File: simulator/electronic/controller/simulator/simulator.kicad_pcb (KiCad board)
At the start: 2 copper layers, 86.9 x 70.1 mm, 57 parts, among them J1 Conn_01x03_Socket, J2 Conn_01x04_Socket, J3 Conn_01x03_Socket, J4 Conn_01x04_Socket, J5 Conn_01x03_Socket, J6 Conn_01x04_Socket, J7 Conn_01x03_Socket, J8 Conn_01x04_Socket, U1 ESP32 D1 Mini

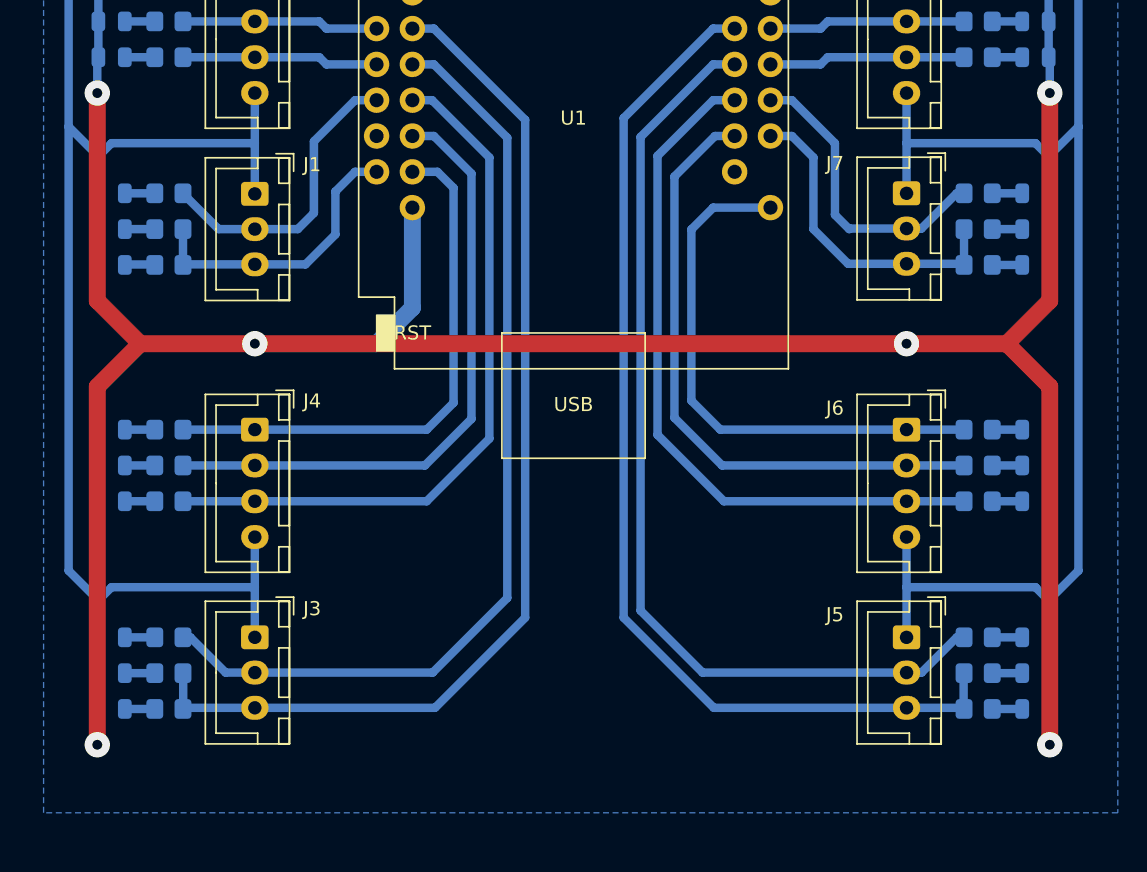
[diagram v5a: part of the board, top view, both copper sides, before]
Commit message: update Platine (Vais)
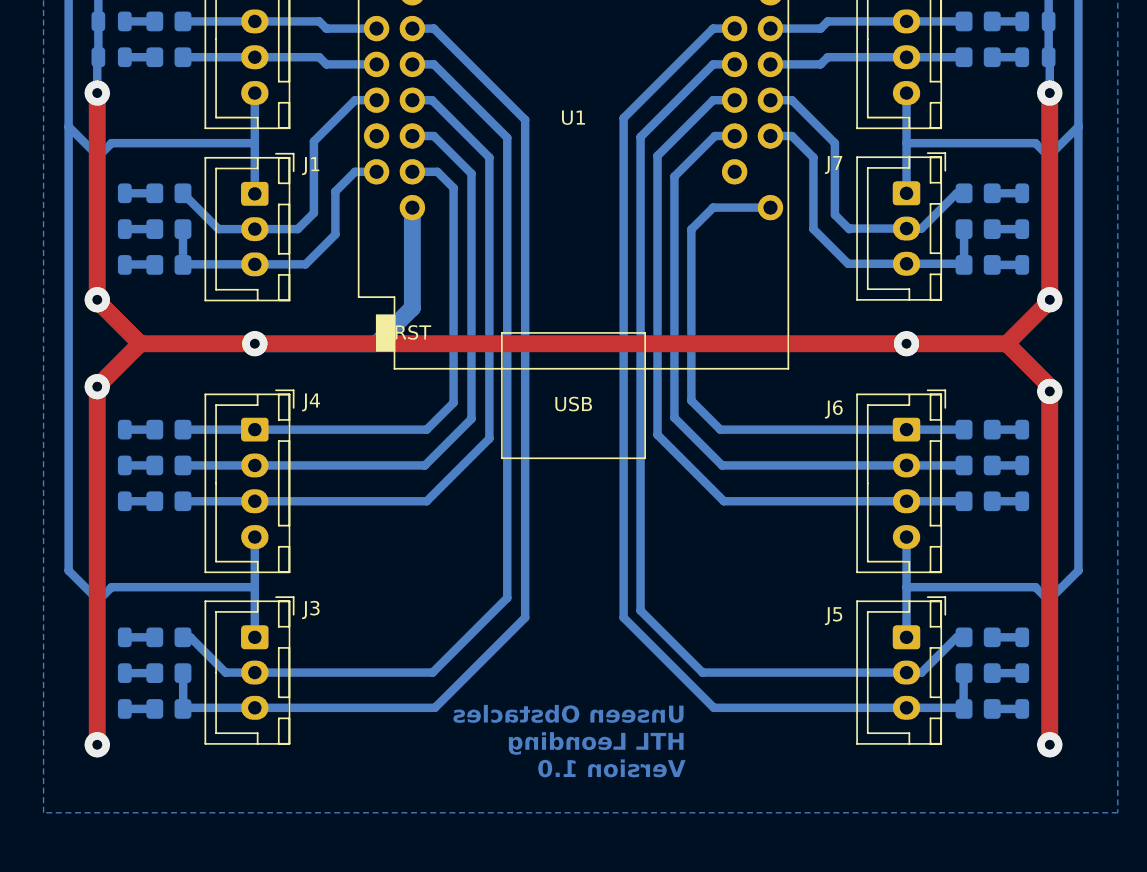
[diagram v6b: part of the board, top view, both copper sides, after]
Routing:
- net 3V3: vias 6 -> 10
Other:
- board text added: "Unseen Obstacles HTL Leonding Version 1.0"
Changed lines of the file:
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@@
 		(layer "Edge.Cuts")
+	)
+	(gr_text "Unseen Obstacles\nHTL Leonding\nVersion 1.0"
+		(at 153.5 133.5 0)
+		(layer "B.Cu")
+		(effects
+			(font
+				(size 1.2 1.2)
+				(thickness 0.2)
+				(bold yes)
+			)
+			(justify left bottom mirror)
+		)
 	)
 	(dimension
@@
 	(segment
 		(start 111.76 99.568)
-		(end 111.76 84.836)
+		(end 111.76 99.5)
+		(width 1.2)
+		(layer "F.Cu")
+		(net 3)
+	)
+	(segment
+		(start 179.324 106)
+		(end 179.324 131.064)
+		(width 1.2)
+		(layer "F.Cu")
+		(net 3)
+	)
+	(segment
+		(start 179.324 99.5)
+		(end 179.324 84.836)
 		(width 1.2)
 		(layer "F.Cu")
@@
 	(segment
 		(start 179.324 105.664)
-		(end 179.324 131.064)
+		(end 179.324 106)
 		(width 1.2)
 		(layer "F.Cu")
@@
 	)
 	(segment
+		(start 111.76 99.5)
+		(end 111.76 84.836)
+		(width 1.2)
+		(layer "F.Cu")
+		(net 3)
+	)
+	(segment
 		(start 122.936 102.616)
 		(end 169.164 102.616)
@@
 	(segment
 		(start 179.324 99.568)
-		(end 179.324 84.836)
+		(end 179.324 99.5)
 		(width 1.2)
 		(layer "F.Cu")
@@
 	)
 	(via
+		(at 111.76 99.5)
+		(size 1.8)
+		(drill 0.7)
+		(layers "F.Cu" "B.Cu")
+		(net 3)
+	)
+	(via
+		(at 179.324 99.5)
+		(size 1.8)
+		(drill 0.7)
+		(layers "F.Cu" "B.Cu")
+		(net 3)
+	)
+	(via
 		(at 111.76 84.836)
 		(size 1.8)
 		(drill 0.7)
+		(layers "F.Cu" "B.Cu")
+		(net 3)
+	)
+	(via
+		(at 111.76 105.664)
+		(size 1.8)
+		(drill 0.7)
+		(layers "F.Cu" "B.Cu")
+		(net 3)
+	)
+	(via
+		(at 179.324 106)
+		(size 1.8)
+		(drill 0.7)

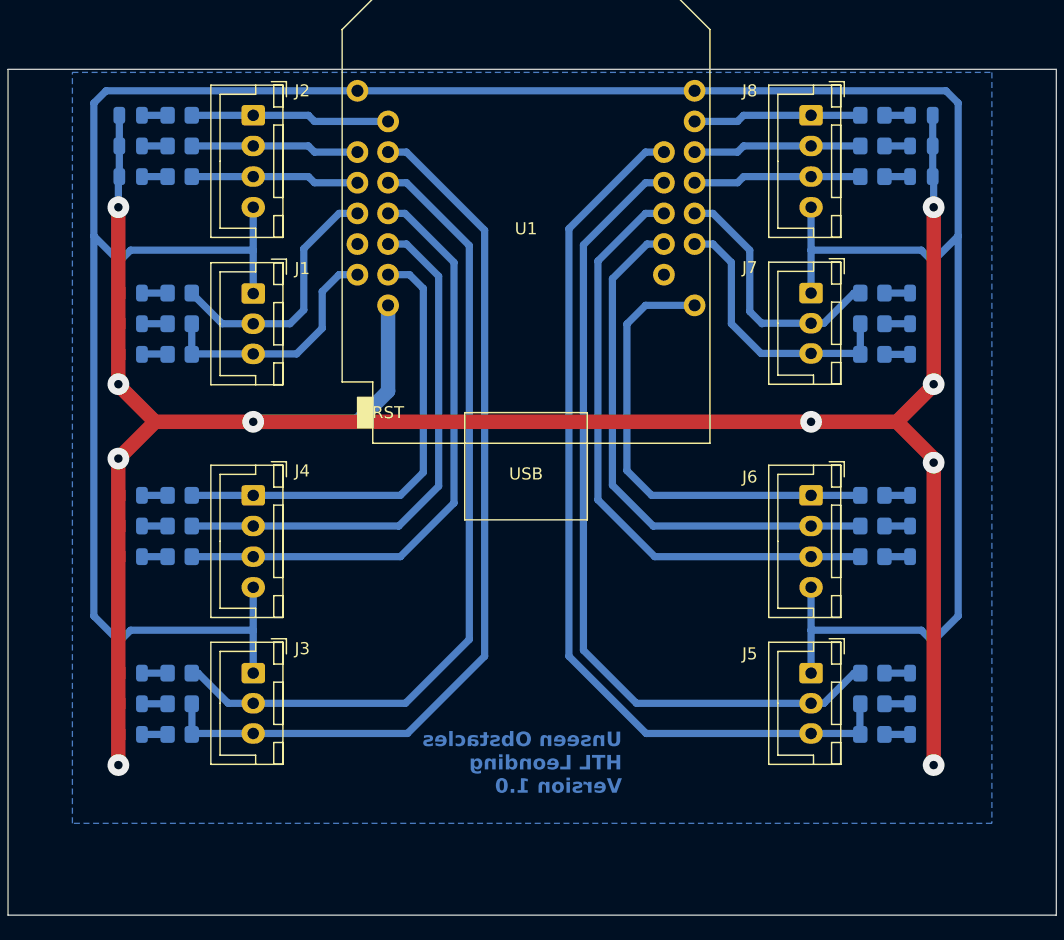
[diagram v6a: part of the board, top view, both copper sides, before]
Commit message: added stabilization Cos and alternative text
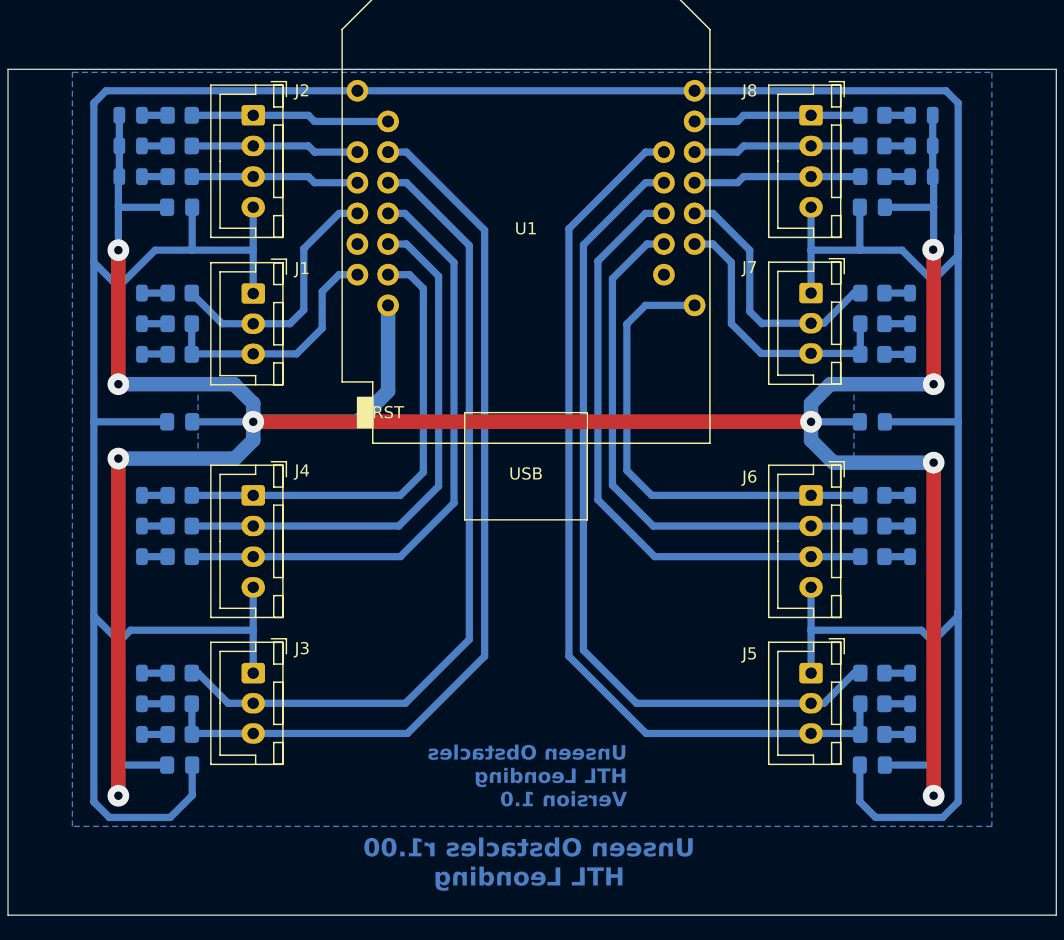
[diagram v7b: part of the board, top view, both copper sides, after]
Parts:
- added C1: 100n, Capacitor_SMD:C_0805_2012Metric_Pad1.18x1.45mm_HandSolder, B.Cu at (116.8, 84.8)
- added C2: 100n, Capacitor_SMD:C_0805_2012Metric_Pad1.18x1.45mm_HandSolder, B.Cu at (116.8, 102.6)
- added C3: 100n, Capacitor_SMD:C_0805_2012Metric_Pad1.18x1.45mm_HandSolder, B.Cu at (116.8, 131.1)
- added C4: 100n, Capacitor_SMD:C_0805_2012Metric_Pad1.18x1.45mm_HandSolder, B.Cu at (174.2, 131.1)
- added C5: 100n, Capacitor_SMD:C_0805_2012Metric_Pad1.18x1.45mm_HandSolder, B.Cu at (174.2, 102.6)
- added C6: 100n, Capacitor_SMD:C_0805_2012Metric_Pad1.18x1.45mm_HandSolder, B.Cu at (174.2, 84.8)
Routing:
- net GND: track 262.5 -> 336.5 mm
- net 3V3: track 252.0 -> 274.6 mm
- added copper zone on B.Cu, net 3V3
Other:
- board text added: "Unseen Obstacles r1.00 HTL Leonding"

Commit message: made PDB singlesided, added stabilization capacitors and label
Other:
- board text removed: "Unseen Obstacles HTL Leonding Version 1.0"
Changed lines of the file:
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@@
 		)
+	)
+	(gr_line
+		(start 184.404 143.51)
+		(end 189.484 143.51)
+		(stroke
+			(width 0.2)
+			(type default)
+		)
+		(layer "B.Cu")
+	)
+	(gr_line
+		(start 189.484 75.692)
+		(end 189.484 73.406)
+		(stroke
+			(width 0.2)
+			(type default)
+		)
+		(layer "B.Cu")
+	)
+	(gr_line
+		(start 102.616 73.406)
+		(end 105.664 73.406)
+		(stroke
+			(width 0.2)
+			(type default)
+		)
+		(layer "B.Cu")
+	)
+	(gr_line
+		(start 189.484 139.446)
+		(end 189.484 143.51)
+		(stroke
+			(width 0.2)
+			(type default)
+		)
+		(layer "B.Cu")
+	)
+	(gr_line
+		(start 102.616 75.946)
+		(end 102.616 73.406)
+		(stroke
+			(width 0.2)
+			(type default)
+		)
+		(layer "B.Cu")
+	)
+	(gr_line
+		(start 102.616 143.51)
+		(end 105.918 143.51)
+		(stroke
+			(width 0.2)
+			(type default)
+		)
+		(layer "B.Cu")
+	)
+	(gr_line
+		(start 102.616 141.097)
+		(end 102.616 143.51)
+		(stroke
+			(width 0.2)
+			(type default)
+		)
+		(layer "B.Cu")
+	)
+	(gr_line
+		(start 186.563 73.406)
+		(end 189.484 73.406)
+		(stroke
+			(width 0.2)
+			(type default)
+		)
+		(layer "B.Cu")
+	)
+	(gr_line
+		(start 105.918 143.51)
+		(end 102.616 143.51)
+		(stroke
+			(width 0.2)
+			(type default)
+		)
+		(layer "B.Cu")
+	)
+	(gr_line
+		(start 189.484 73.406)
+		(end 186.563 73.406)
+		(stroke
+			(width 0.2)
+			(type default)
+		)
+		(layer "B.Cu")
+	)
+	(gr_line
+		(start 105.664 73.406)
+		(end 102.616 73.406)
+		(stroke
+			(width 0.2)
+			(type default)
+		)
+		(layer "B.Cu")
+	)
+	(gr_line
+		(start 189.484 143.51)
+		(end 189.484 139.446)
+		(stroke
+			(width 0.2)
+			(type default)
+		)
+		(layer "B.Cu")
 	)
 	(gr_rect
@@
 		(fill no)
 		(layer "Edge.Cuts")
-	)
-	(gr_text "Unseen Obstacles\nHTL Leonding\nVersion 1.0"
-		(at 153.924 134.62 0)
-		(layer "B.Cu" knockout)
-		(effects
-			(font
-				(size 1.2 1.2)
-				(thickness 0.2)
-				(bold yes)
-			)
-			(justify left bottom mirror)
-		)
 	)
 	(gr_text "Unseen Obstacles r1.00\nHTL Leonding"
@@
 			(xy 102.616 143.5) (xy 189.49 143.5)
 		)
-		(height -2.53)
+		(height 2.296)
 		(orientation 0)
 		(format
@@
 		)
 		(gr_text "86,874"
-			(at 146.053 139.82 0)
+			(at 146.053 144.646 0)
 			(layer "User.4")
 			(effects
@@
 			(xy 102.616 73.406) (xy 102.616 143.5)
 		)
-		(height 2.794)
+		(height -2.54)
 		(orientation 1)
 		(format
@@
 		)
 		(gr_text "70,094"
-			(at 104.26 108.453 90)
+			(at 98.926 108.453 90)
 			(layer "User.4")
 			(effects
